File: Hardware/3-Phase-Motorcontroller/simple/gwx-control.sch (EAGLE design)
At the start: 11 parts, among them IC1 74LS02N

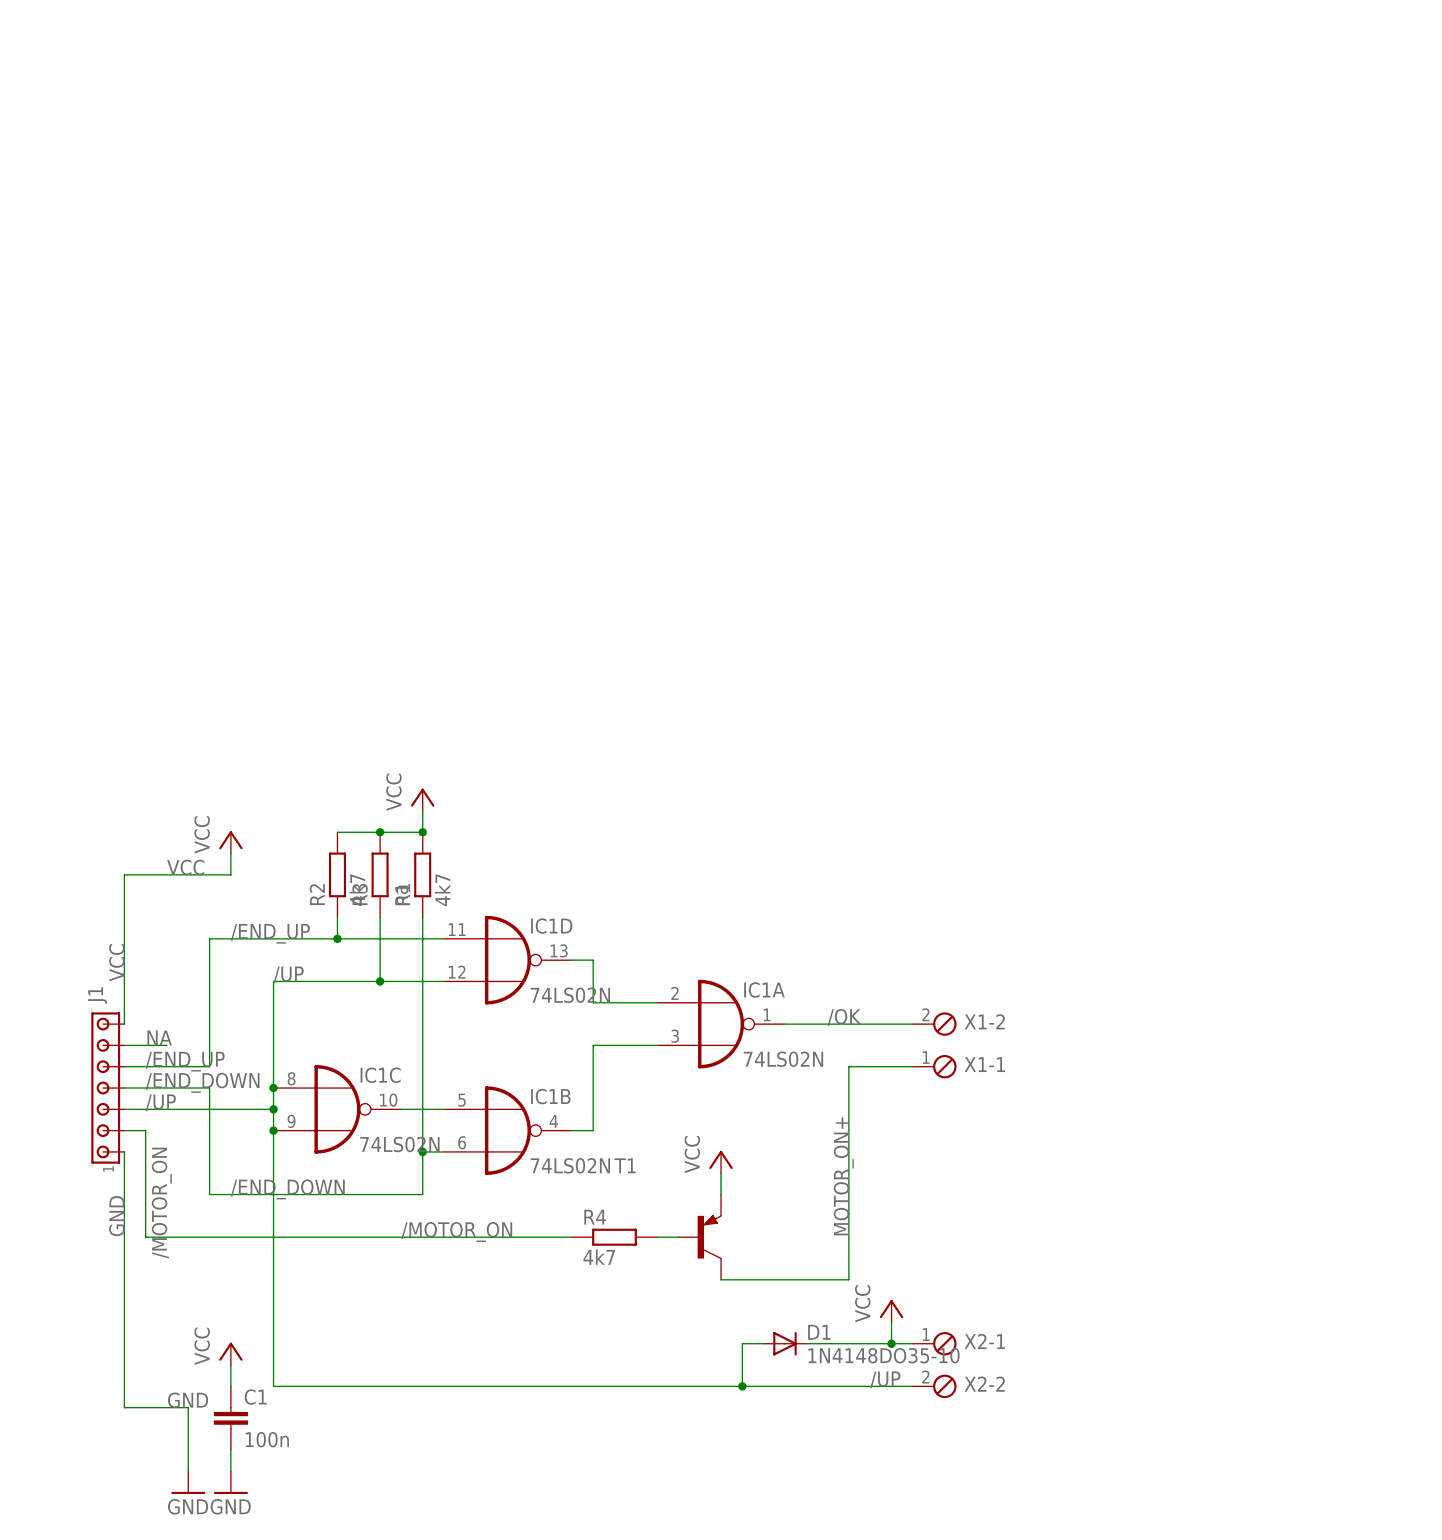
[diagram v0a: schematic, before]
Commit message: added power switch protection
motor will stop for a few seconds, if direction changes
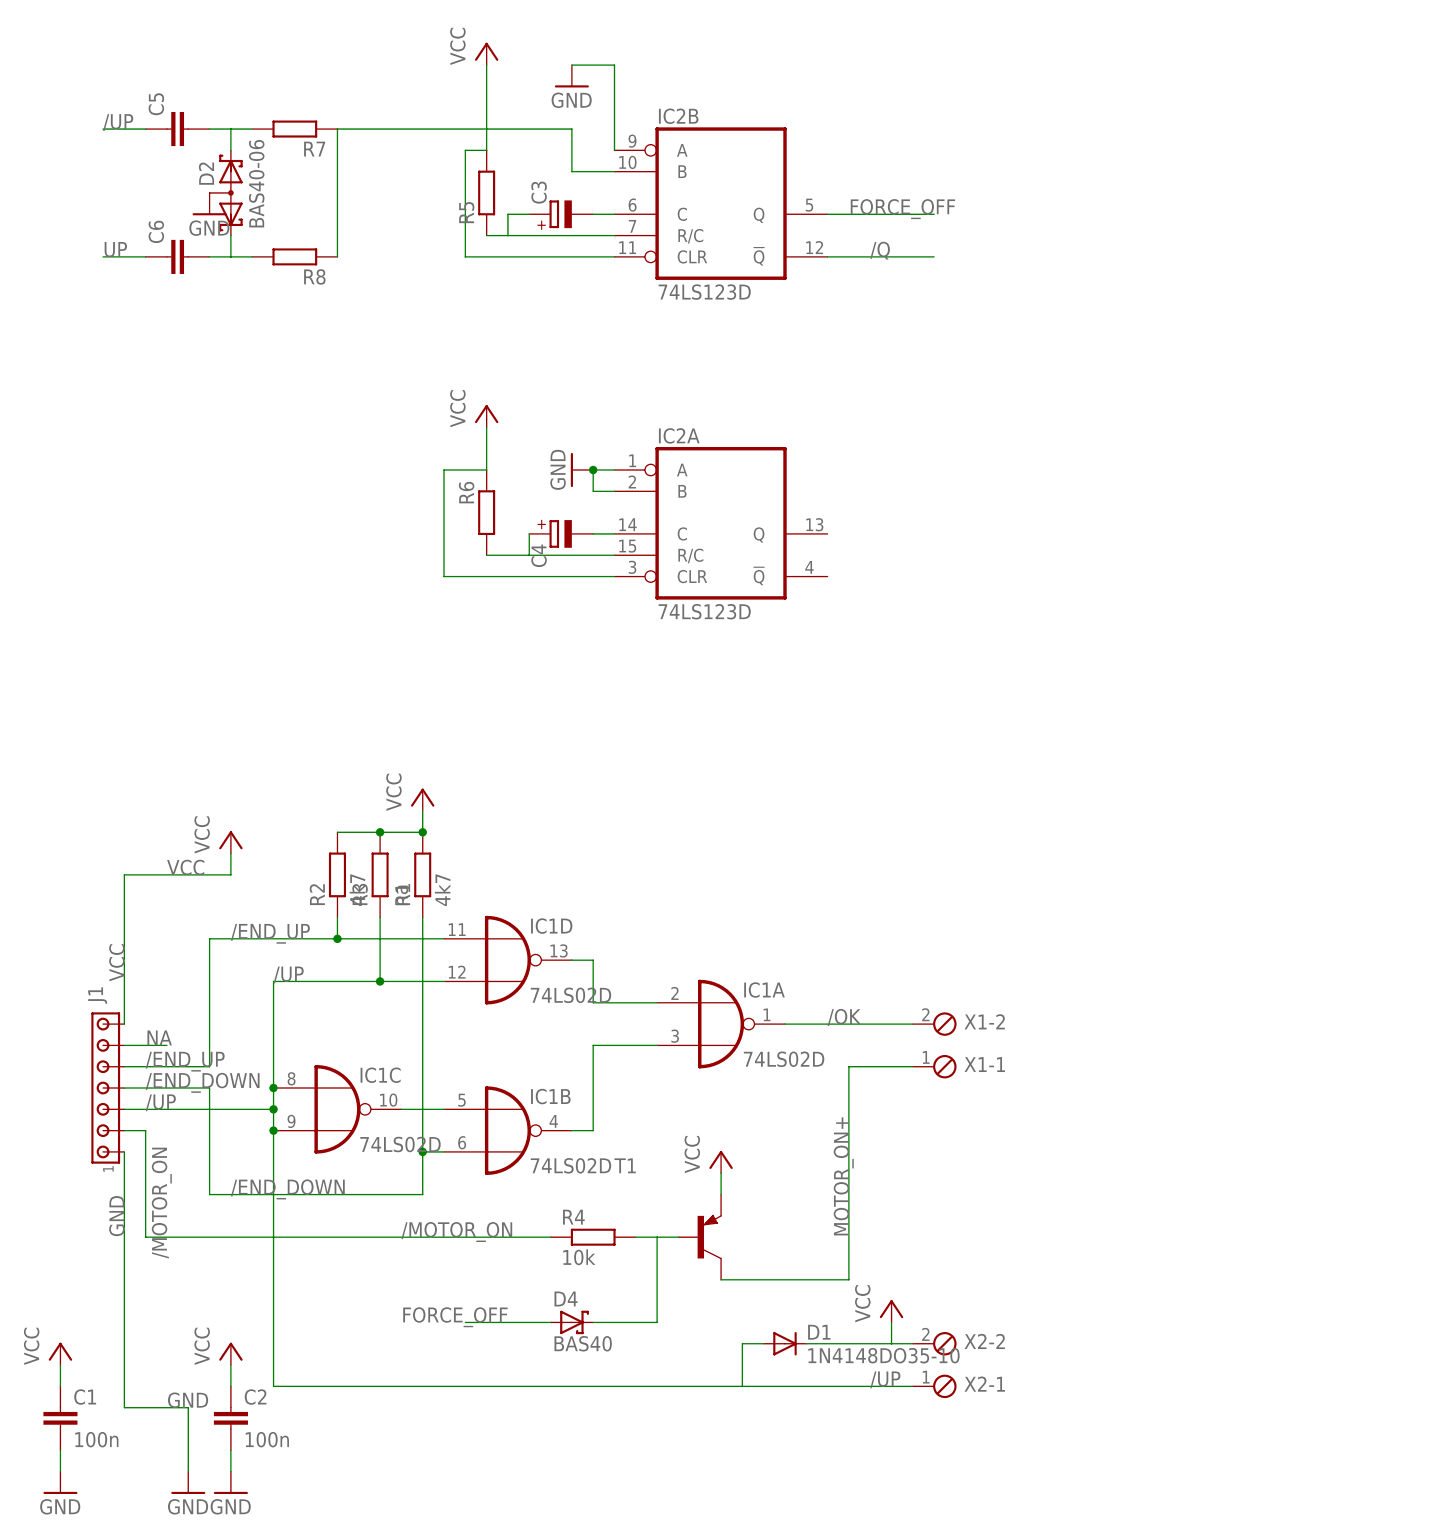
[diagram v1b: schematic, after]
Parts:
- added C2: 100n, rcl:C-EUC0603K
- added C3, C4: (no value), rcl:CPOL-EUE5-6
- added C5, C6: (no value), rcl:C-EUC0603K
- added D2: BAS40-06, diode:BAS40-06
- added D4: BAS40, diode:BAS40
- added IC2: 74LS123D, 74xx-eu:74LS123D
- added R5, R6, R7, R8: (no value), rcl:R-EU_R0603
- C1: device capacitor-wima:C5/2.5 -> rcl:C-EUC0603K
- IC1: value 74LS02N -> 74LS02D; device 74xx-eu:74LS02N -> 74xx-eu:74LS02D
- R4: value 4k7 -> 10k
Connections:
- new net /Q: IC2B.!Q
- new net FORCE_OFF: D4.A, IC2B.Q
- new net N$10: D4.C, R4.2, T1.B
- new net N$2: C3.-, IC2B.C
- new net N$4: C5.2, D2.K2, R7.2
- new net N$7: C6.2, D2.K1, R8.2
- new net N$8: IC2B.B, R7.1, R8.1
- new net N$9: C4.-, IC2A.C
- new net UP: C6.1, IC1B.I0, IC1C.O
- net /UP: now also C5.1, X2-1.1; no longer X2-2.1
- net GND: now also C2.2, D2.AA, IC2A.A, IC2A.B, IC2B.A
- net N$1: now also C3.+, IC2B.R/C, R5.1; no longer IC1B.I0, IC1C.O
- net N$3: now also C4.+, IC2A.R/C, R6.2; no longer R4.2, T1.B
- net VCC: now also C2.1, IC2A.CLR, IC2B.CLR, R5.2, R6.1, X2-2.1; no longer X2-1.1
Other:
- moved on the sheet: C1, R4, X2-1, X2-2

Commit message: Trigger fixed
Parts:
- removed D2: BAS40-06, diode:BAS40-06
- added D3: BAT54C, diode:BAT54C
- added R9: 47k, rcl:R-EU_R0603
- C3: value (none) -> 47µ
- R5, R7, R8: value (none) -> 47k
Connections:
- net GND: now also R7.2, R8.1, R9.2; no longer D2.AA
- net N$4: now also D3.A2, R7.1; no longer D2.K2, R7.2
- net N$7: now also D3.A1; no longer D2.K1
- net N$8: now also D3.CC, R9.1; no longer R7.1, R8.1
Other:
- note added: "Unused"
- moved on the sheet: C3, C4, C5, C6, IC2A, IC2B, R5, R6, R7, R8

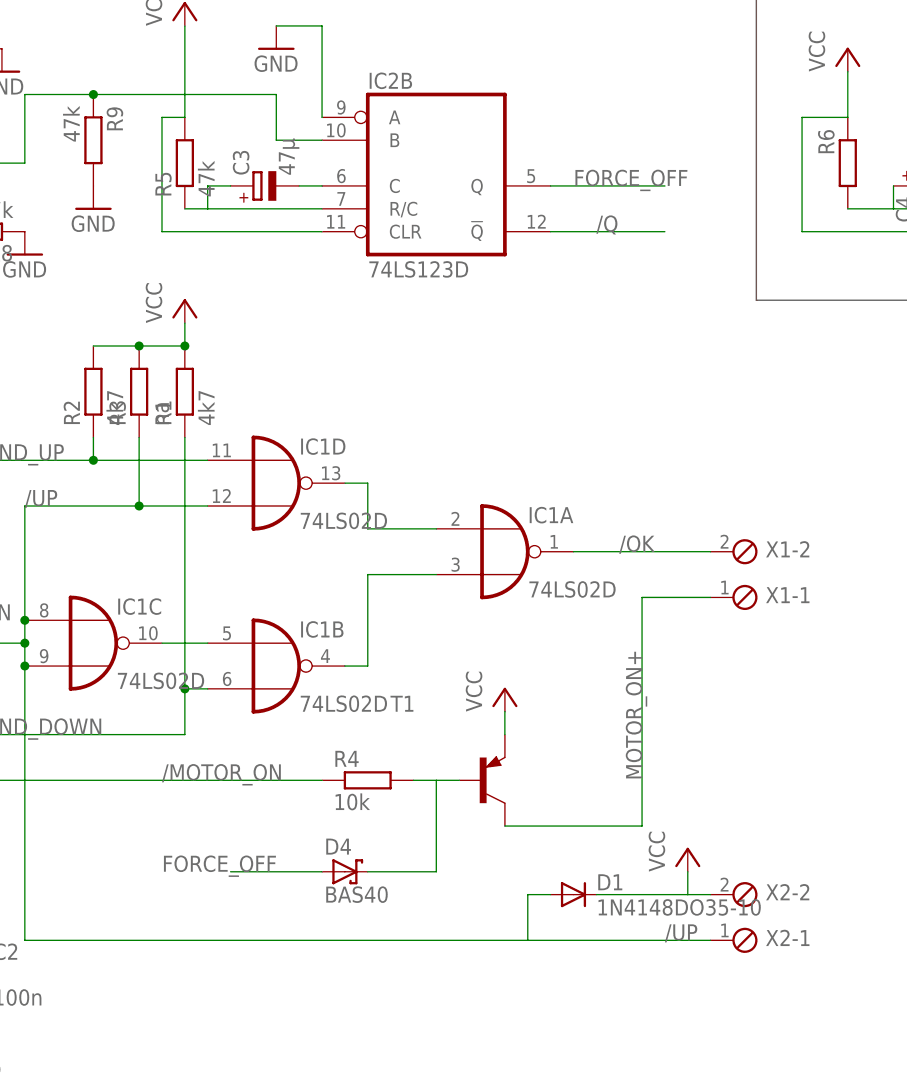
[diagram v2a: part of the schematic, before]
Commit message: force motor off is now more relyable
changed from pull down the base of t1 to active switch a 2n T in series
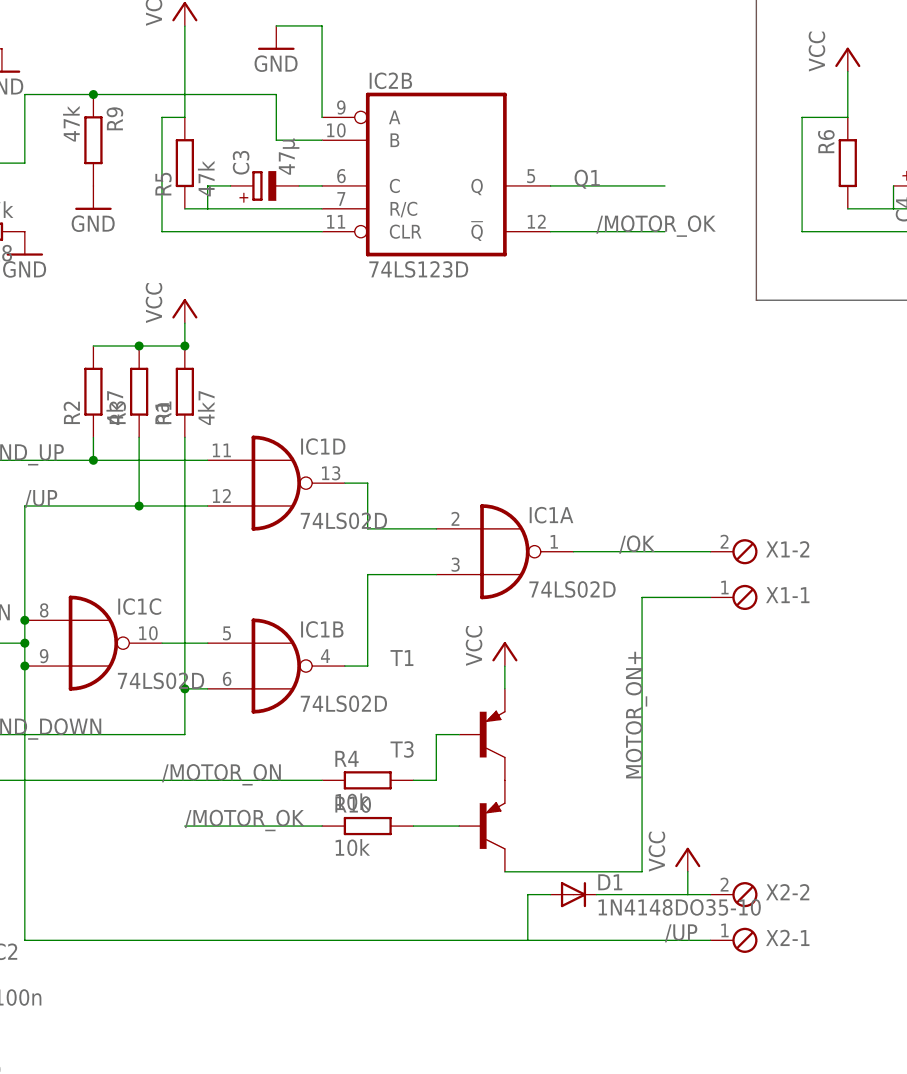
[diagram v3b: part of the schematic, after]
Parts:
- removed D4: BAS40, diode:BAS40
- added R10: 10k, resistor:R-EU_R0603
- added T3: (no value), transistor:BC856B-PNP-SOT23-BEC
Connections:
- removed net /Q: IC2B.!Q
- removed net FORCE_OFF: D4.A, IC2B.Q
- new net /MOTOR_OK: IC2B.!Q, R10.1
- new net N$11: R4.2, T1.B
- new net N$12: T1.C, T3.E
- new net Q1: IC2B.Q
- net MOTOR_ON+: now also T3.C; no longer T1.C
- net N$10: now also R10.2, T3.B; no longer D4.C, R4.2, T1.B
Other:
- moved on the sheet: T1
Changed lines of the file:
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@@
 <part name="P+8" library="supply1" deviceset="VCC" device=""/>
 <part name="GND6" library="supply1" deviceset="GND" device=""/>
-<part name="D4" library="diode" deviceset="BAS40" device=""/>
 <part name="D3" library="diode" deviceset="BAT54C" device=""/>
 <part name="R7" library="rcl" deviceset="R-EU_" device="R0603" value="47k"/>
@@
 <part name="R9" library="rcl" deviceset="R-EU_" device="R0603" value="47k"/>
 <part name="GND8" library="supply1" deviceset="GND" device=""/>
+<part name="T3" library="transistor" deviceset="*-PNP-" device="SOT23-BEC" technology="BC856B"/>
+<part name="R10" library="resistor" deviceset="R-EU_" device="R0603" value="10k"/>
 </parts>
 <sheets>
@@
 <instance part="P+4" gate="VCC" x="25.4" y="93.98"/>
 <instance part="R4" gate="G$1" x="45.72" y="40.64"/>
-<instance part="T1" gate="G$1" x="58.42" y="40.64"/>
-<instance part="P+5" gate="VCC" x="60.96" y="50.8"/>
+<instance part="T1" gate="G$1" x="58.42" y="45.72"/>
+<instance part="P+5" gate="VCC" x="60.96" y="55.88"/>
 <instance part="C2" gate="G$1" x="2.54" y="20.32"/>
 <instance part="IC2" gate="A" x="127" y="109.22"/>
@@
 <instance part="P+8" gate="VCC" x="99.06" y="121.92"/>
 <instance part="GND6" gate="1" x="109.22" y="114.3" rot="R270"/>
-<instance part="D4" gate="1" x="43.18" y="30.48"/>
 <instance part="D3" gate="G$1" x="-5.08" y="109.22" rot="R270"/>
 <instance part="R7" gate="G$1" x="0" y="121.92"/>
@@
 <instance part="R9" gate="G$1" x="15.24" y="111.76" rot="R270"/>
 <instance part="GND8" gate="1" x="15.24" y="104.14"/>
+<instance part="T3" gate="G$1" x="58.42" y="35.56"/>
+<instance part="R10" gate="G$1" x="45.72" y="35.56"/>
 </instances>
 <busses>
@@
 <pinref part="T1" gate="G$1" pin="E"/>
 <pinref part="P+5" gate="VCC" pin="VCC"/>
-<wire x1="60.96" y1="48.26" x2="60.96" y2="45.72" width="0.1524" layer="91"/>
+<wire x1="60.96" y1="53.34" x2="60.96" y2="50.8" width="0.1524" layer="91"/>
 </segment>
 <segment>
@@
 <pinref part="X1" gate="-1" pin="1"/>
 <wire x1="83.82" y1="60.96" x2="76.2" y2="60.96" width="0.1524" layer="91"/>
-<wire x1="76.2" y1="60.96" x2="76.2" y2="35.56" width="0.1524" layer="91"/>
-<pinref part="T1" gate="G$1" pin="C"/>
-<wire x1="76.2" y1="35.56" x2="60.96" y2="35.56" width="0.1524" layer="91"/>
+<wire x1="76.2" y1="60.96" x2="76.2" y2="30.48" width="0.1524" layer="91"/>
 <label x="76.2" y="40.64" size="1.778" layer="95" rot="R90"/>
+<pinref part="T3" gate="G$1" pin="C"/>
+<wire x1="60.96" y1="30.48" x2="76.2" y2="30.48" width="0.1524" layer="91"/>
 </segment>
 </net>
@@
 </segment>
 </net>
-<net name="N$10" class="0">
-<segment>
-<pinref part="T1" gate="G$1" pin="B"/>
-<pinref part="R4" gate="G$1" pin="2"/>
-<wire x1="50.8" y1="40.64" x2="53.34" y2="40.64" width="0.1524" layer="91"/>
-<wire x1="53.34" y1="40.64" x2="55.88" y2="40.64" width="0.1524" layer="91"/>
-<wire x1="53.34" y1="30.48" x2="53.34" y2="40.64" width="0.1524" layer="91"/>
-<pinref part="D4" gate="1" pin="C"/>
-<wire x1="45.72" y1="30.48" x2="53.34" y2="30.48" width="0.1524" layer="91"/>
-</segment>
-</net>
-<net name="/Q" class="0">
-<segment>
-<pinref part="IC2" gate="B" pin="!Q"/>
-<wire x1="66.04" y1="101.6" x2="78.74" y2="101.6" width="0.1524" layer="91"/>
-<label x="71.12" y="101.6" size="1.778" layer="95"/>
-</segment>
-</net>
 <net name="N$3" class="0">
 <segment>
@@
 </segment>
 </net>
-<net name="FORCE_OFF" class="0">
+<net name="N$11" class="0">
+<segment>
+<pinref part="T1" gate="G$1" pin="B"/>
+<pinref part="R4" gate="G$1" pin="2"/>
+<wire x1="50.8" y1="40.64" x2="53.34" y2="40.64" width="0.1524" layer="91"/>
+<wire x1="53.34" y1="40.64" x2="53.34" y2="45.72" width="0.1524" layer="91"/>
+<wire x1="53.34" y1="45.72" x2="55.88" y2="45.72" width="0.1524" layer="91"/>
+</segment>
+</net>
+<net name="N$12" class="0">
+<segment>
+<pinref part="T1" gate="G$1" pin="C"/>
+<pinref part="T3" gate="G$1" pin="E"/>
+</segment>
+</net>
+<net name="N$10" class="0">
+<segment>
+<pinref part="R10" gate="G$1" pin="2"/>
+<pinref part="T3" gate="G$1" pin="B"/>
+<wire x1="50.8" y1="35.56" x2="55.88" y2="35.56" width="0.1524" layer="91"/>
+</segment>
+</net>
+<net name="/MOTOR_OK" class="0">
+<segment>
+<pinref part="R10" gate="G$1" pin="1"/>
+<wire x1="40.64" y1="35.56" x2="25.4" y2="35.56" width="0.1524" layer="91"/>
+<label x="25.4" y="35.56" size="1.778" layer="95"/>
+</segment>
+<segment>
+<pinref part="IC2" gate="B" pin="!Q"/>
+<wire x1="66.04" y1="101.6" x2="78.74" y2="101.6" width="0.1524" layer="91"/>
+<label x="71.12" y="101.6" size="1.778" layer="95"/>
+</segment>
+</net>
+<net name="Q1" class="0">
 <segment>
 <pinref part="IC2" gate="B" pin="Q"/>
@@
 <label x="68.58" y="106.68" size="1.778" layer="95"/>
 </segment>
-<segment>
-<pinref part="D4" gate="1" pin="A"/>
-<wire x1="40.64" y1="30.48" x2="30.48" y2="30.48" width="0.1524" layer="91"/>
-<label x="22.86" y="30.48" size="1.778" layer="95"/>
-</segment>
-</net>
+</net>
